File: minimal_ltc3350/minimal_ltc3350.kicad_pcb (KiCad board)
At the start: 4 copper layers, 59.7 x 49.5 mm, 85 parts, among them Q1 20.0 V, Q2 20.0 V, Q3 20 V, Q4 20 V, Q5 20.0 V, Q6 8 V, Q7 8 V, Q8 8 V, Q9 8 V, U1 LTC3350EUHF-PBF

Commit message: feat: Update KiCad project and symbols
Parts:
- R1: value 0.016 Ω -> 16 mΩ
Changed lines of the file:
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@@
 			)
 		)
-		(property "Value" "0.016 Ω"
+		(property "Value" "16 mΩ"
 			(at 0 2.54 0)
 			(unlocked yes)
@@
 			)
 		)
-		(property "Datasheet" "https://www.susumu.co.jp/common/pdf/n_catalog_partition07_en.pdf"
+		(property "Datasheet" "https://industrial.panasonic.com/cdbs/www-data/pdf/RDN0000/AOA0000C325.pdf"
 			(at 0 0 0)
 			(layer "F.Fab")
@@
 			)
 		)
-		(property "Description" "RES SMD 0.016 Ω 1% 0612"
+		(property "Description" "RES SMD 16 mΩ 1% 0612"
 			(at 0 0 0)
 			(layer "F.Fab")
@@
 			)
 		)
-		(property "MPN" "PRL1632-R016-F-T1"
+		(property "MPN" "ERJ-B2CFR016V"
 			(at 0 0 0)
 			(unlocked yes)
@@
 			)
 		)
-		(property "Manufacturer" "Susumu"
+		(property "Manufacturer" "Panasonic"
 			(at 0 0 0)
 			(unlocked yes)
@@
 			)
 		)
-		(property "Series" "PRL1632-"
+		(property "Series" "ERJ-B2CF"
 			(at 0 0 0)
 			(unlocked yes)
@@
 			)
 		)
-		(property "Symbol Name" "R_PRL1632-R016-F-T1"
+		(property "Symbol Name" "R_ERJ-B2CFR016V"
 			(at 0 0 0)
 			(unlocked yes)
@@
 			)
 		)
-		(property "Trustedparts Search" "https://www.trustedparts.com/en/search/PRL1632-R016-F-T1"
+		(property "Trustedparts Search" "https://www.trustedparts.com/en/search/ERJ-B2CFR016V"
 			(at 0 0 0)
 			(unlocked yes)

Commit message: Update KiCad PCB and schematic files
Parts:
- R3: value 665 kΩ -> 909 Ω
- R4: value 162 kΩ -> 100 kΩ
- R9: value 0.006 Ω -> 6 mΩ
- moved R19 2.90 mm to (141.4, 95.6), turned to 0 degrees
- moved C3 1.31 mm to (132.7, 92.2)
- moved R4 1.31 mm to (132.7, 90.9)
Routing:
- net /CAP4: track 5.97 -> 3.48 mm
- net /VOUT: track 33.6 -> 36.0 mm, vias 15 -> 16

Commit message: Update KiCad project files
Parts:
- moved C11 5.79 mm to (152.7, 73.4)
- moved C12 5.79 mm to (152.7, 78.1)
- moved C13 5.79 mm to (152.7, 79.4)
- moved Q3 5.79 mm to (154.8, 82.4)
- moved Q4 5.79 mm to (150.9, 82.4)
- moved C10 5.79 mm to (152.7, 76.1)
- moved L1 5.79 mm to (152.9, 88.9)
- moved R1 5.62 mm to (144.7, 82.8)
- moved Q1 4.21 mm to (145.1, 78.3), turned to -90 degrees
- moved Q2 2.48 mm to (145.1, 99.5)
- moved C9 2.31 mm to (142.5, 95.0), turned to 90 degrees
- moved C2 2.31 mm to (142.5, 82.8), turned to -90 degrees
- moved R9 1.95 mm to (144.7, 95.0)
- moved Q5 1.83 mm to (136.8, 99.6)
- moved R28 1.83 mm to (131.8, 105.4)
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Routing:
- net /VOUT: track 36.0 -> 27.0 mm
- net /BGATE: track 15.3 -> 20.6 mm
- net /VOUTSP: track 10.3 -> 5.31 mm
- net /TGATE: track 13.0 -> 18.0 mm
- net /VCC2P5: track 20.1 -> 23.3 mm
- net /VCAP: track 21.7 -> 18.6 mm
- net /OUTFET: track 15.4 -> 13.5 mm
- net /INFET: track 9.85 -> 11.5 mm
- net /ICAP: track 8.30 -> 6.76 mm
- net /INTVCC: track 19.2 -> 18.1 mm
- net /ITST: track 10.5 -> 11.1 mm
- net /CAP2: track 16.3 -> 15.7 mm
- net /CFP: track 1.67 -> 2.18 mm
- net GND: track 0.00 -> 0.08 mm, vias 40 -> 44

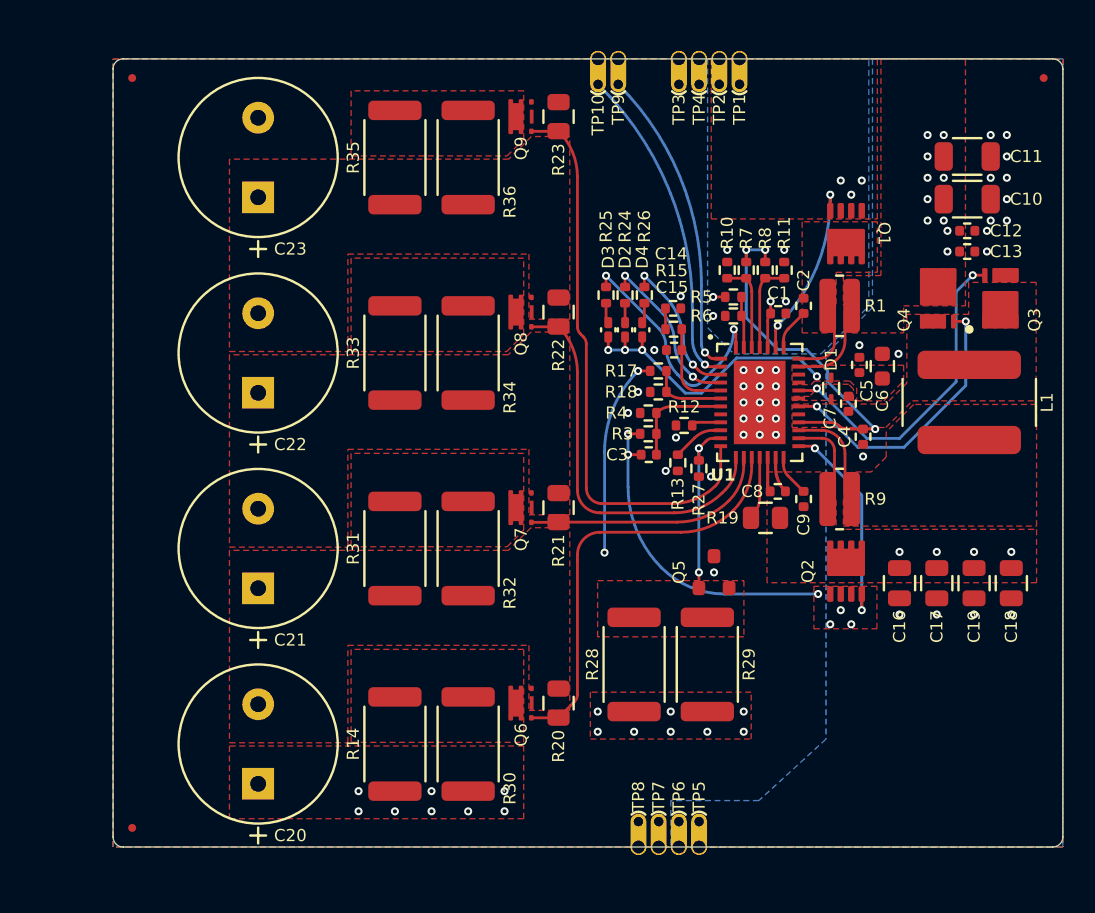
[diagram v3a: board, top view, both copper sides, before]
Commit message: Update KiCAD project files: Remove component properties and adjust zone connections
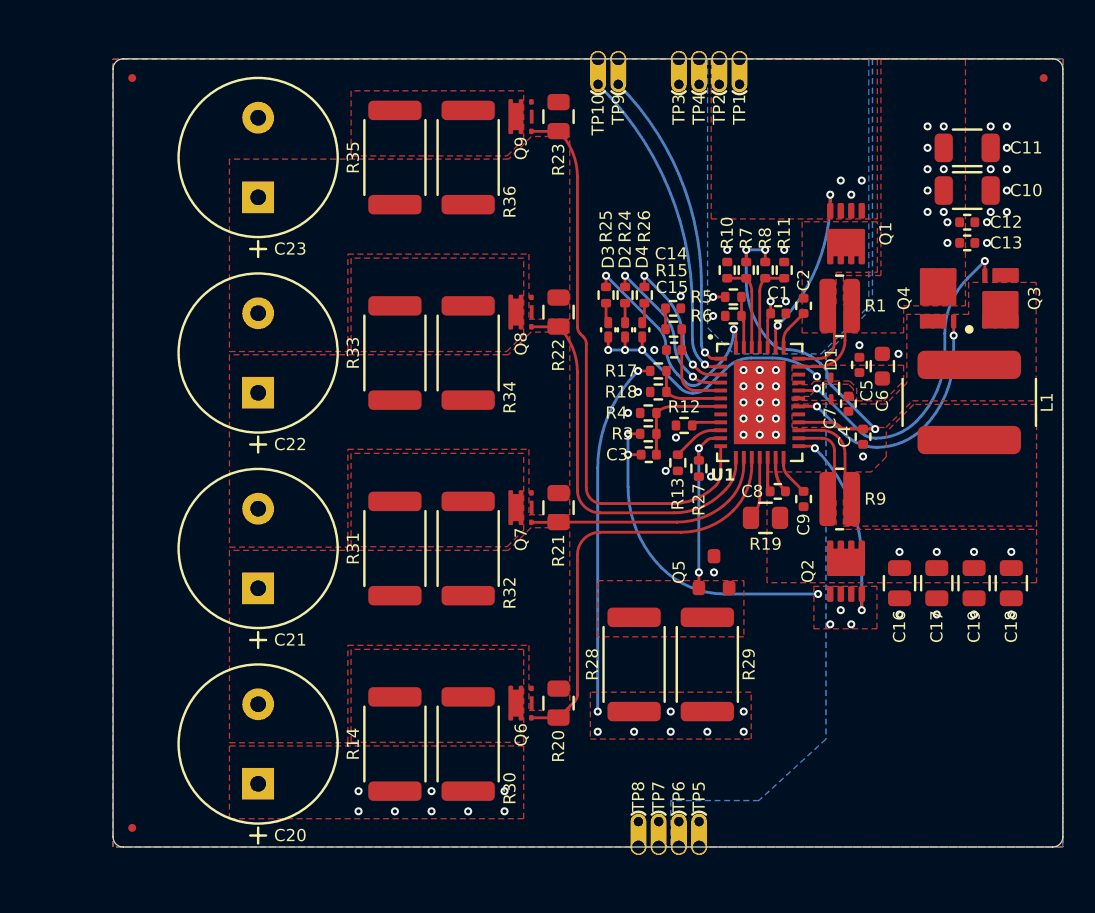
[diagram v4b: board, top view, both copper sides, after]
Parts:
- moved C10 0.54 mm to (152.7, 75.6)
- moved C13 0.54 mm to (152.7, 78.9)
- moved C11 0.54 mm to (152.7, 72.9)
- moved C12 0.54 mm to (152.7, 77.6)
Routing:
- net /VCAP: track 18.6 -> 28.7 mm, vias 22 -> 21
- net /TGATE: track 18.0 -> 16.2 mm
- net /BGATE: track 20.6 -> 21.1 mm
- net /VCC2P5: track 23.3 -> 22.7 mm

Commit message: Update KiCad schematic and PCB files
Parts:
- added J1: CLP-102-02-G-D-BE, connector_footprints:CLP-102-02-G-D-BE, F.Cu at (111.6, 110.4)
- added J2: CLP-102-02-G-D-BE, connector_footprints:CLP-102-02-G-D-BE, F.Cu at (111.6, 101.2)
- added J3: CLP-102-02-G-D-BE, connector_footprints:CLP-102-02-G-D-BE, F.Cu at (111.6, 91.9)
- added J4: CLP-102-02-G-D-BE, connector_footprints:CLP-102-02-G-D-BE, F.Cu at (111.6, 82.7)
- added J5: CLP-102-02-G-D-BE, connector_footprints:CLP-102-02-G-D-BE, F.Cu at (111.6, 73.5)
- moved C20 7.62 mm to (100.6, 110.4)
- moved C21 7.62 mm to (100.6, 98.1)
- moved C22 7.62 mm to (100.6, 85.8)
- moved C23 7.62 mm to (100.6, 73.5)
- moved FID1 5.08 mm to (95.2, 115.6)
- moved FID2 5.08 mm to (95.2, 68.5)
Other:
- board size 59.7 x 49.5 mm -> 64.8 x 49.5 mm

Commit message: Update KiCad project files: PCB layout, project settings, and schematic
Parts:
- removed C20, C21, C22, C23: 10 F, capacitor_footprints:C_197x394_H31_5_5_0x10Metric
- moved FID1 17.9 mm to (113.0, 117.8)
- moved FID2 17.8 mm to (113.0, 67.0)
- moved TP3 14.4 mm to (148.6, 70.7)
- moved TP4 11.9 mm to (147.3, 70.7)
- moved TP10 10.7 mm to (139.7, 70.7)
- moved TP9 10.7 mm to (141.0, 70.7)
- moved TP5 10.6 mm to (146.1, 113.9)
- moved TP6 10.6 mm to (144.8, 113.9)
- moved TP7 10.6 mm to (143.5, 113.9)
- moved TP8 10.6 mm to (142.2, 113.9)
- moved TP2 9.52 mm to (146.1, 70.7)
- moved J1 7.50 mm to (117.2, 115.4), turned to -90 degrees
- moved TP1 7.20 mm to (144.8, 70.7)
- moved J5 7.05 mm to (117.2, 69.2), turned to -90 degrees
- moved J2 6.19 mm to (117.2, 103.8), turned to -90 degrees
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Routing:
- net /SDA: track 20.4 -> 16.5 mm
- net /SCL: track 19.4 -> 16.1 mm
- net /CAPRTN: track 36.1 -> 34.6 mm
- net /CAP3: track 26.9 -> 26.1 mm
- net /CAP1: track 24.9 -> 24.3 mm
- removed copper zone on B.Cu, net /VIN
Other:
- board size 64.8 x 49.5 mm -> 47 x 53.3 mm

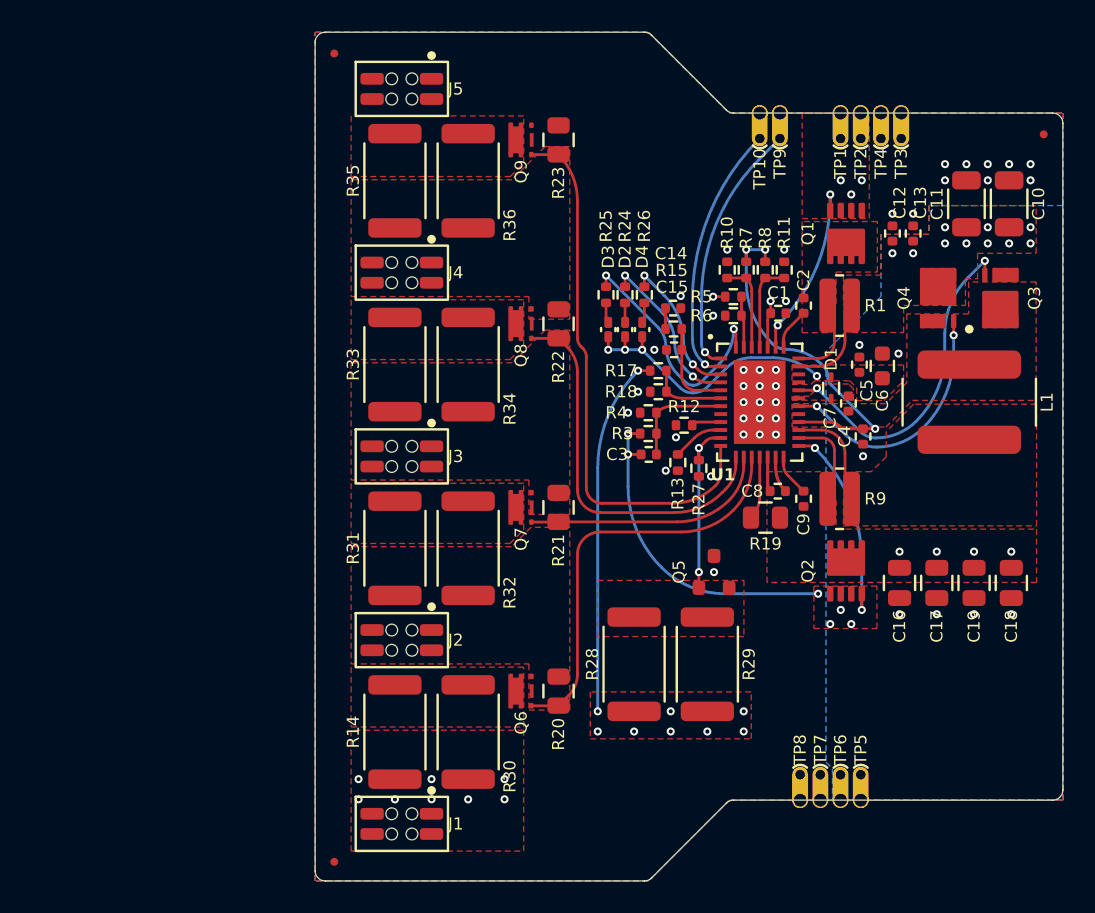
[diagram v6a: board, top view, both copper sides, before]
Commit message: Update KiCAD Symbols Generator and PCB layout changes
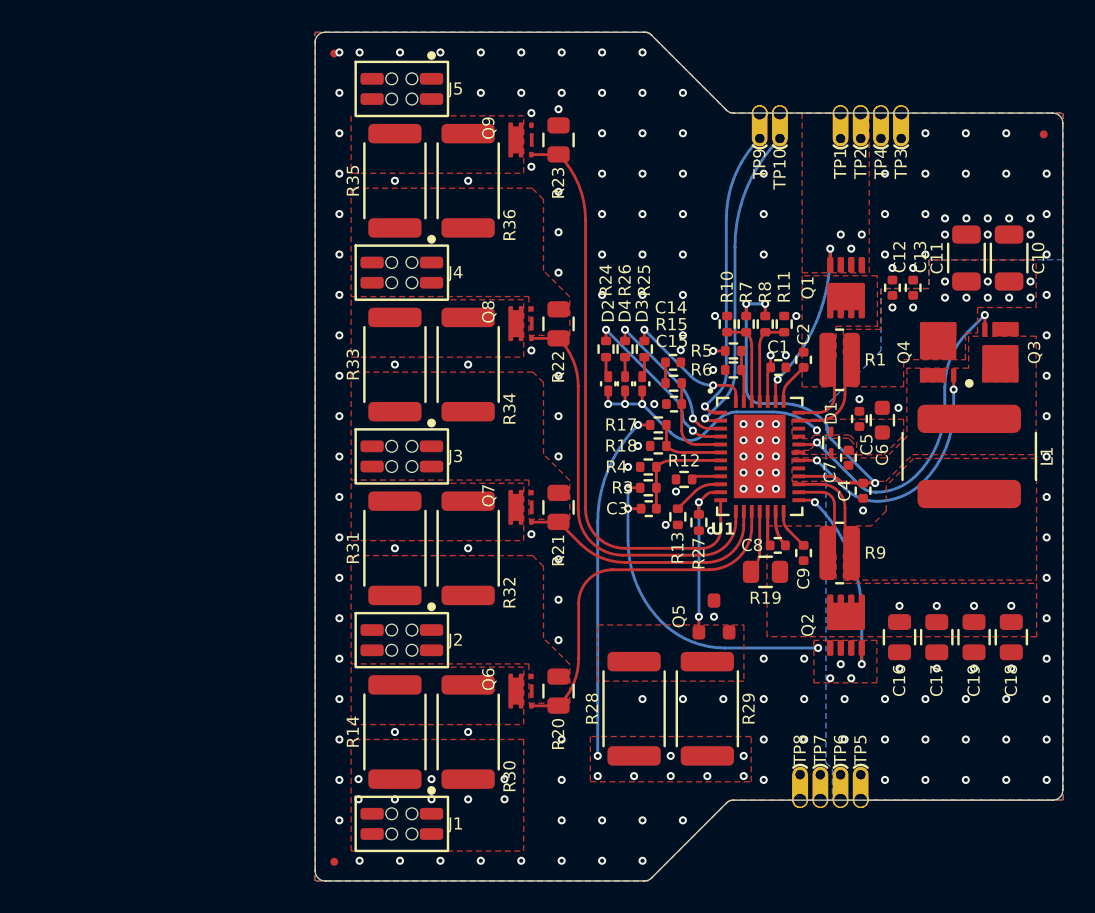
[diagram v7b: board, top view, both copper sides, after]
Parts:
- moved R25 4.17 mm to (132.5, 85.5)
- moved D3 4.02 mm to (132.3, 87.7)
- moved R26 3.62 mm to (131.2, 85.5)
- moved R24 3.61 mm to (130.0, 85.5)
- moved D4 3.57 mm to (131.2, 87.7)
- moved D2 3.57 mm to (130.2, 87.7)
- moved C10 3.41 mm to (155.4, 79.8)
- moved C11 3.41 mm to (152.7, 79.8)
- moved C12 3.41 mm to (148.0, 81.7)
- moved C13 3.41 mm to (149.3, 81.7)
- moved C14 3.41 mm to (134.3, 86.4)
- moved C16 3.41 mm to (148.5, 103.7)
- moved C17 3.41 mm to (150.8, 103.7)
- moved C18 3.41 mm to (155.5, 103.7)
- moved C19 3.41 mm to (153.2, 103.7)
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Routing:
- net /~{PFO}: track 15.6 -> 8.57 mm
- net /SDA: track 16.5 -> 20.0 mm
- net /CAP3: track 26.1 -> 22.9 mm
- net /SCL: track 16.1 -> 19.0 mm
- net /CAPRTN: track 34.6 -> 36.7 mm
- net /CAP1: track 24.3 -> 26.0 mm
- net /VCC2P5: track 22.7 -> 23.8 mm
- net /~{SMBALERT}: track 9.21 -> 9.86 mm
- net /CAPGD: track 10.4 -> 11.0 mm
- net /CAP2: track 15.7 -> 16.3 mm
- net /ITST: track 11.1 -> 10.5 mm
- net /VCAP: track 28.7 -> 28.1 mm
- net GND: vias 44 -> 184

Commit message: Update KiCAD project files: PCB and schematic
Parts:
- added C3: 1 µF, capacitor_footprints:C_0402_1005Metric, F.Cu at (148.0, 81.7)
- added C6: 1 µF, capacitor_footprints:C_0402_1005Metric, F.Cu at (140.9, 85.1)
- moved R18 1.32 mm to (133.3, 90.3)
- moved R19 1.32 mm to (133.3, 91.6)
- moved C4 1.30 mm to (149.3, 81.7)
- moved C5 1.30 mm to (150.6, 81.7)
- moved R4 0.96 mm to (137.7, 83.0)
- moved R5 0.96 mm to (138.9, 83.0)
- moved R6 0.96 mm to (140.0, 83.0)
- moved R7 0.96 mm to (141.2, 83.0)
- moved Q7 0.80 mm to (136.6, 101.6)
- moved R31 0.80 mm to (131.6, 107.4)
- moved R32 0.80 mm to (136.2, 107.4)
- moved C2 0.51 mm to (155.9, 79.8)
- moved C1 0.51 mm to (153.2, 79.8)
- moved R24 0.36 mm to (134.6, 96.4)
- moved R9 0.28 mm to (138.0, 85.4)
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- renumbered C11 to C1, C15 to C10, C5 to C11, C6 to C12, C7 to C13, C4 to C14, C3 to C15, C8 to C16, C9 to C17, C16 to C18, C17 to C19, C10 to C2, C19 to C20, C18 to C21, C12 to C4, C13 to C5, C2 to C7, C14 to C8, C1 to C9, D2 to D1, D4 to D2, D1 to D4, FID2 to FID1, FID3 to FID2, FID1 to FID3, J5 to J1, J4 to J2, J2 to J4, J1 to J5, Q9 to Q1, Q1 to Q2, Q8 to Q3, Q3 to Q5, Q7 to Q6, Q5 to Q7, Q2 to Q8, Q6 to Q9, R23 to R1, R24 to R10, R26 to R11, R25 to R12, R1 to R13, R33 to R14, R34 to R15, R6 to R16, R15 to R17, R17 to R19, R35 to R2, R4 to R20, R12 to R21, R3 to R22, R21 to R23, R13 to R24, R27 to R25, R31 to R26, R32 to R27, R9 to R28, R19 to R29, R36 to R3, R20 to R30, R28 to R31, R29 to R32, R14 to R33, R30 to R34, R10 to R4, R7 to R5, R8 to R6, R11 to R7, R22 to R8, R5 to R9, TP9 to TP1, TP5 to TP10, TP10 to TP2, TP1 to TP3, TP2 to TP4, TP4 to TP5, TP3 to TP6, TP8 to TP7, TP7 to TP8, TP6 to TP9
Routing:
- net /VCAP: track 28.1 -> 20.2 mm, vias 21 -> 23
- net /INTVCC: track 17.3 -> 23.6 mm
- net /BGATE: track 21.1 -> 17.1 mm
- net /TGATE: track 16.2 -> 13.8 mm
- net /VCC2P5: track 23.8 -> 21.5 mm
- net /VIN: track 3.71 -> 5.36 mm, vias 5 -> 6
- net /CAP_SLCT1: track 5.63 -> 6.59 mm
- net /CAP_SLCT0: track 5.63 -> 6.59 mm
- net /~{PFO}: track 8.57 -> 9.50 mm
- net /ITST: track 10.5 -> 10.0 mm
- net GND: vias 184 -> 185
- net /VOUT: vias 16 -> 17
